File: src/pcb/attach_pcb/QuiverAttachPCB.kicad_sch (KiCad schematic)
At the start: 21 parts, among them J1 2077601281

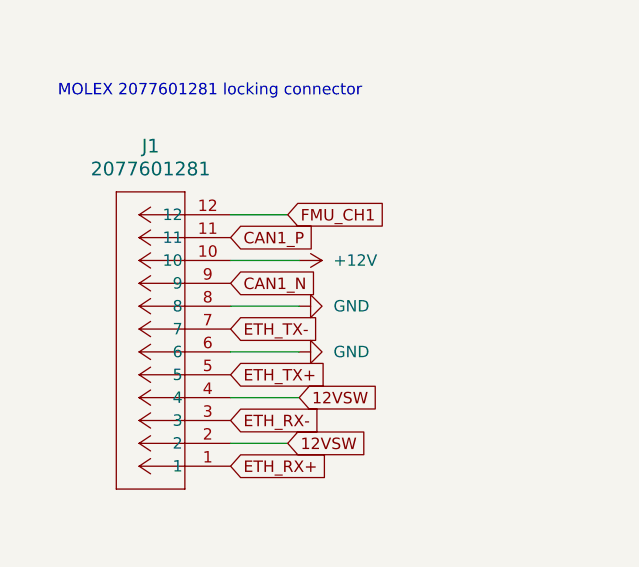
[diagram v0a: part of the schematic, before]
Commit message: fix: add PWR_FLAG to +12V and GND in attach_pcb schematic
ERC reports two power_pin_not_driven errors on QuiverAttachPCB (#PWR01 on
+12V and #PWR04 on GND): both nets enter through connectors, whose pins
are passive, so no power output pin drives them. Add one PWR_FLAG on each
net, joined by a short wire to the existing power symbols.

Schematic-only change: 252 lines added, none removed. The .kicad_pcb and
the project files are untouched, so there is no electrical or layout change.

Co-Authored-By: Claude Sonnet 5.5 <noreply@anthropic.com>
Signed-off-by: Alan Rosas Palacios <43190667+trimaxlan98@users.noreply.github.com>
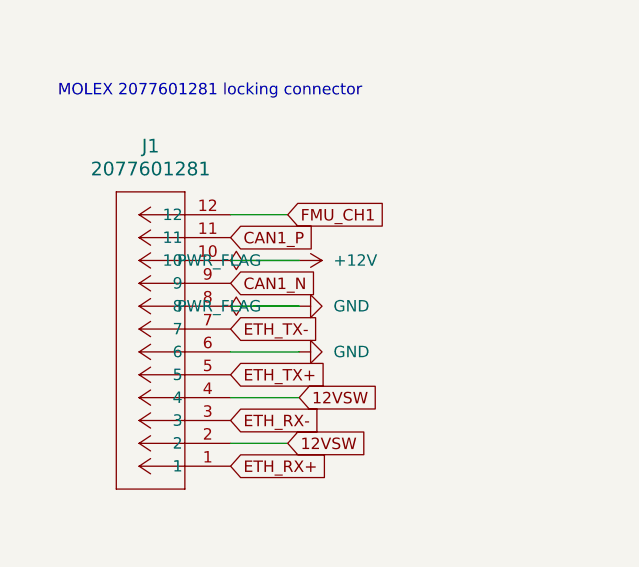
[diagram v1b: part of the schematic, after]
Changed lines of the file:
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@@
+		)
+	)
+	(wire
+		(pts
+			(xy 81.28 99.06) (xy 86.36 99.06)
+		)
+		(stroke
+			(width 0)
+			(type default)
+		)
+	)
+	(symbol
+		(lib_id "power:PWR_FLAG")
+		(at 81.28 99.06 90)
+		(unit 1)
+		(exclude_from_sim no)
+		(in_bom yes)
+		(on_board yes)
+		(dnp no)
+		(property "Reference" "#FLG01"
+			(at 81.28 99.06 0)
+			(effects
+				(font
+					(size 1.27 1.27)
+				)
+				(hide yes)
+			)
+		)
+		(property "Value" "PWR_FLAG"
+			(at 77.47 99.06 90)
+			(effects
+				(font
+					(size 1.27 1.27)
+				)
+			)
+		)
+		(property "Footprint" ""
+			(at 81.28 99.06 0)
+			(effects
+				(font
+					(size 1.27 1.27)
+				)
+				(hide yes)
+			)
+		)
+		(property "Datasheet" "~"
+			(at 81.28 99.06 0)
+			(effects
+				(font
+					(size 1.27 1.27)
+				)
+				(hide yes)
+			)
+		)
+		(property "Description" "Special symbol for telling ERC where power comes from"
+			(at 81.28 99.06 0)
+			(effects
+				(font
+					(size 1.27 1.27)
+				)
+				(hide yes)
+			)
+		)
+		(pin "1"
+		)
+		(instances
+			(project "QuiverAttachPCB"
+				(path "/faf6ae05-859a-4da4-87ce-2d178afa08f0"
+					(reference "#FLG01")
+					(unit 1)
+				)
+			)
+		)
+	)
+	(wire
+		(pts
+			(xy 81.28 104.14) (xy 86.36 104.14)
+		)
+		(stroke
+			(width 0)
+			(type default)
+		)
+	)
+	(symbol
+		(lib_id "power:PWR_FLAG")
+		(at 81.28 104.14 90)
+		(unit 1)
+		(exclude_from_sim no)
+		(in_bom yes)
+		(on_board yes)
+		(dnp no)
+		(property "Reference" "#FLG02"
+			(at 81.28 104.14 0)
+			(effects
+				(font
+					(size 1.27 1.27)
+				)
+				(hide yes)
+			)
+		)
+		(property "Value" "PWR_FLAG"
+			(at 77.47 104.14 90)
+			(effects
+				(font
+					(size 1.27 1.27)
+				)
+			)
+		)
+		(property "Footprint" ""
+			(at 81.28 104.14 0)
+			(effects
+				(font
+					(size 1.27 1.27)
+				)
+				(hide yes)
+			)
+		)
+		(property "Datasheet" "~"
+			(at 81.28 104.14 0)
+			(effects
+				(font
+					(size 1.27 1.27)
+				)
+				(hide yes)
+			)
+		)
+		(property "Description" "Special symbol for telling ERC where power comes from"
+			(at 81.28 104.14 0)
+			(effects
+				(font
+					(size 1.27 1.27)
+				)
+				(hide yes)
+			)
+		)
+		(pin "1"
+		)
+		(instances
+			(project "QuiverAttachPCB"
+				(path "/faf6ae05-859a-4da4-87ce-2d178afa08f0"
+					(reference "#FLG02")
+					(unit 1)
+				)
+			)
 		)
 	)
